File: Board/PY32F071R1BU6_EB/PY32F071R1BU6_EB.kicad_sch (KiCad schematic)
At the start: 2 parts, among them J7 Conn_02x05_Odd_Even, U1 PY32F071R1BU

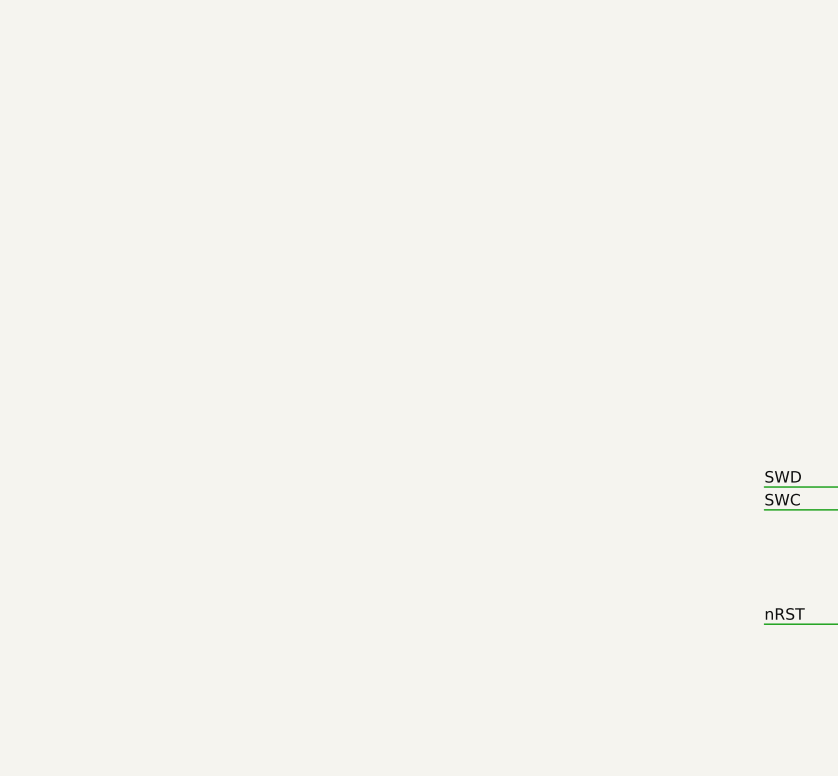
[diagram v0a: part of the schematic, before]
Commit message: Added USB connector
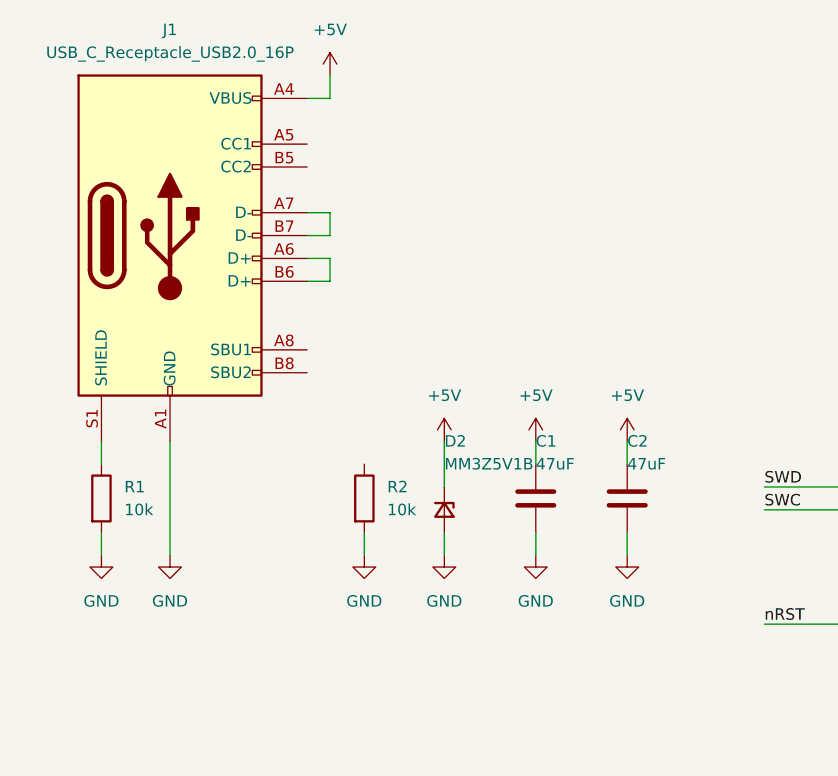
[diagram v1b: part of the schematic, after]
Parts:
- added C1, C2: 47uF, Capacitor_SMD:C_0805_2012Metric_Pad1.18x1.45mm_HandSolder, symbol Device:C
- added D2: MM3Z5V1B, Diode_SMD:D_SOD-323, symbol Device:D_Zener_Small
- added J1: USB_C_Receptacle_USB2.0_16P, Connector_USB:USB_C_Receptacle_HCTL_HC-TYPE-C-16P-01A, symbol Connector:USB_C_Receptacle_USB2.0_16P
- added R1, R2: 10k, Resistor_SMD:R_0603_1608Metric_Pad0.98x0.95mm_HandSolder, symbol Device:R
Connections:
- net +5V: now also C1.1, C2.1, D2.1 (K), J1.A4 (VBUS), J1.A9 (VBUS), J1.B4 (VBUS), J1.B9 (VBUS)
- net GND: now also C1.2, C2.2, D2.2 (A), J1.A1 (GND), J1.A12 (GND), J1.B1 (GND), J1.B12 (GND), R1.2, R2.2
- new net: J1.A6 (D+), J1.B6 (D+)
- new net: J1.A7 (D-), J1.B7 (D-)
- new net: J1.S1 (SHIELD), R1.1

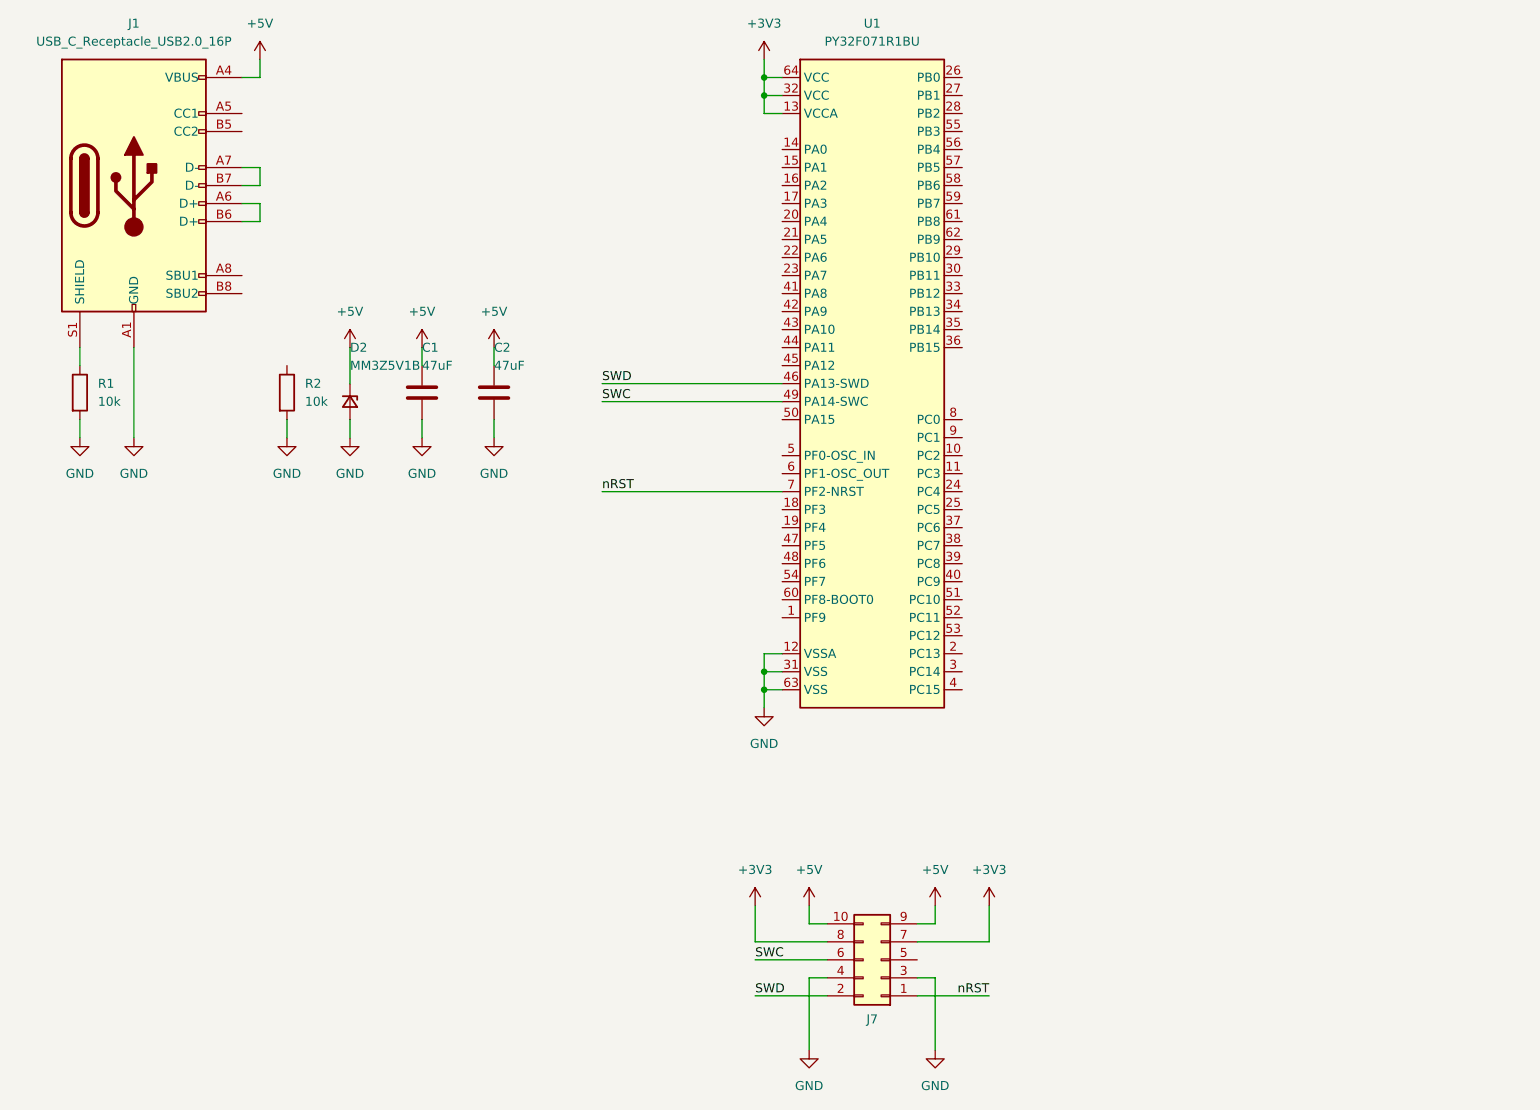
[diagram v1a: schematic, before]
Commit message: Kicad project was split in hierarchical sheets
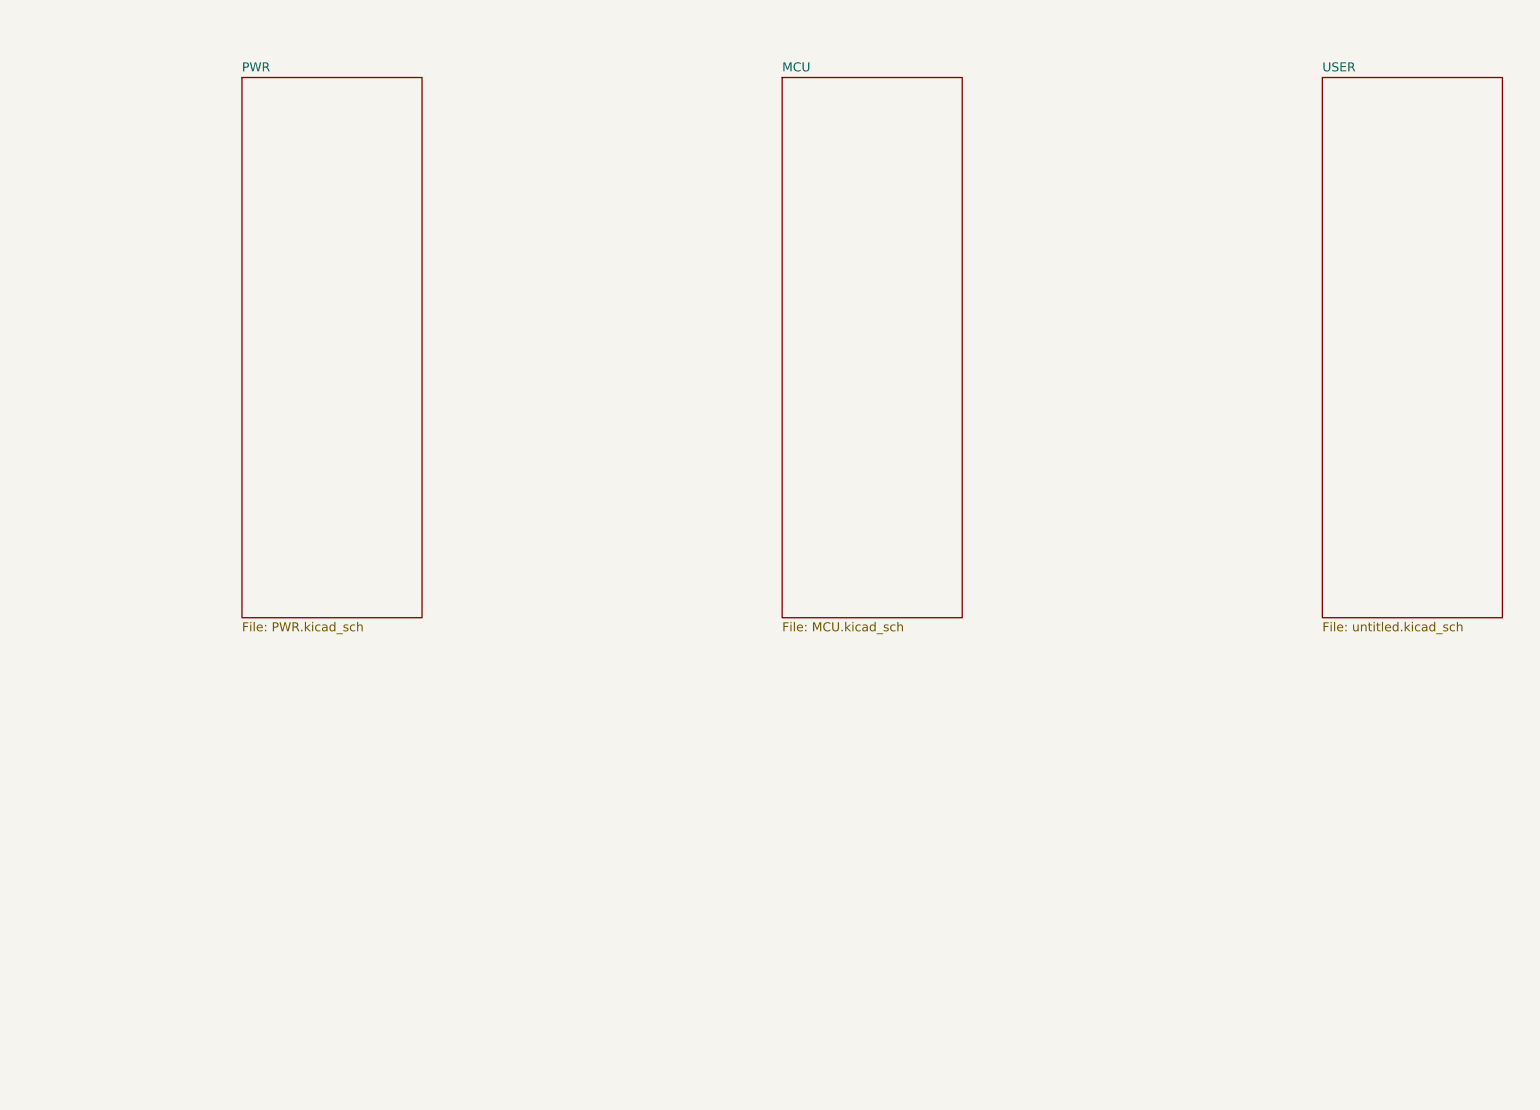
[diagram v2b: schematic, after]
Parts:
- removed C1, C2: 47uF, Capacitor_SMD:C_0805_2012Metric_Pad1.18x1.45mm_HandSolder, symbol Device:C
- removed D2: MM3Z5V1B, Diode_SMD:D_SOD-323, symbol Device:D_Zener_Small
- removed J1: USB_C_Receptacle_USB2.0_16P, Connector_USB:USB_C_Receptacle_HCTL_HC-TYPE-C-16P-01A, symbol Connector:USB_C_Receptacle_USB2.0_16P
- removed J7: Conn_02x05_Odd_Even, Connector_IDC:IDC-Header_2x05_P2.54mm_Vertical, symbol Connector_Generic:Conn_02x05_Odd_Even
- removed R1, R2: 10k, Resistor_SMD:R_0603_1608Metric_Pad0.98x0.95mm_HandSolder, symbol Device:R
- removed U1: PY32F071R1BU, Package_DFN_QFN:QFN-64-1EP_8x8mm_P0.4mm_EP6.5x6.5mm, symbol USER:PY32F071R1BU6
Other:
- added sheet MCU (MCU.kicad_sch)
- added sheet PWR (PWR.kicad_sch)
- added sheet USER (untitled.kicad_sch)

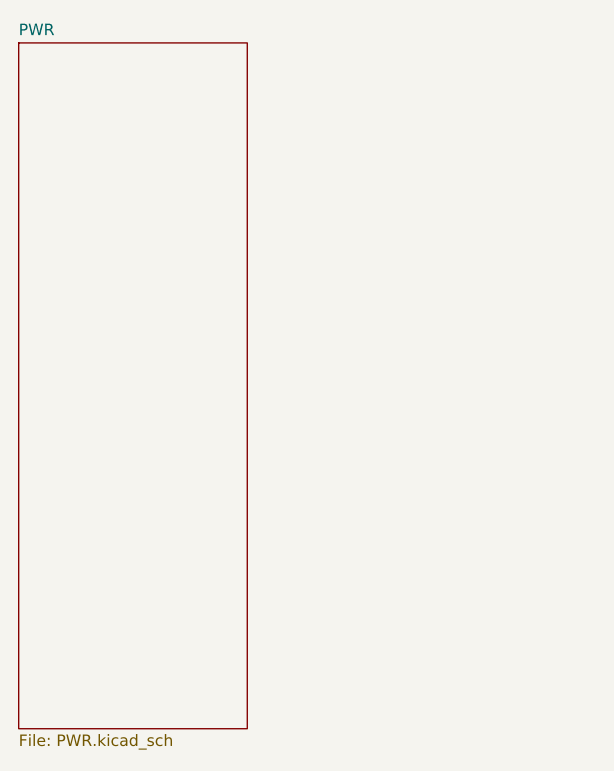
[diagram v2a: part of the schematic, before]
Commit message: Power circuit prepared
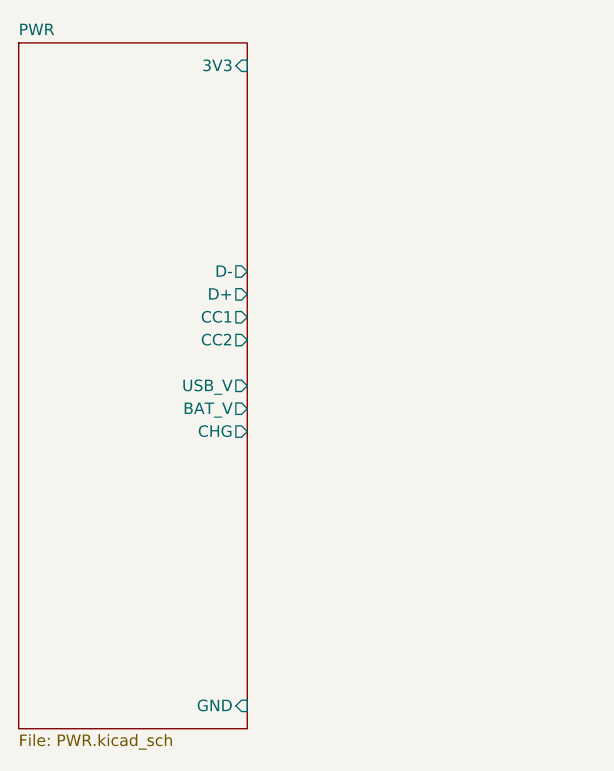
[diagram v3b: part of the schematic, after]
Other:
- sheet PWR ports: added 3V3, BAT_V, CC1, CC2, CHG, D+, D-, GND, USB_V; removed none
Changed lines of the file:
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@@
+			)
+		)
+		(pin "3V3" input
+			(at 76.2 53.34 0)
+			(effects
+				(font
+					(size 1.27 1.27)
+				)
+				(justify right)
+			)
+		)
+		(pin "GND" input
+			(at 76.2 124.46 0)
+			(effects
+				(font
+					(size 1.27 1.27)
+				)
+				(justify right)
+			)
+		)
+		(pin "D-" output
+			(at 76.2 76.2 0)
+			(effects
+				(font
+					(size 1.27 1.27)
+				)
+				(justify right)
+			)
+		)
+		(pin "D+" output
+			(at 76.2 78.74 0)
+			(effects
+				(font
+					(size 1.27 1.27)
+				)
+				(justify right)
+			)
+		)
+		(pin "CC2" output
+			(at 76.2 83.82 0)
+			(effects
+				(font
+					(size 1.27 1.27)
+				)
+				(justify right)
+			)
+		)
+		(pin "CC1" output
+			(at 76.2 81.28 0)
+			(effects
+				(font
+					(size 1.27 1.27)
+				)
+				(justify right)
+			)
+		)
+		(pin "CHG" output
+			(at 76.2 93.98 0)
+			(effects
+				(font
+					(size 1.27 1.27)
+				)
+				(justify right)
+			)
+		)
+		(pin "USB_V" output
+			(at 76.2 88.9 0)
+			(effects
+				(font
+					(size 1.27 1.27)
+				)
+				(justify right)
+			)
+		)
+		(pin "BAT_V" output
+			(at 76.2 91.44 0)
+			(effects
+				(font
+					(size 1.27 1.27)
+				)
+				(justify right)
 			)
 		)

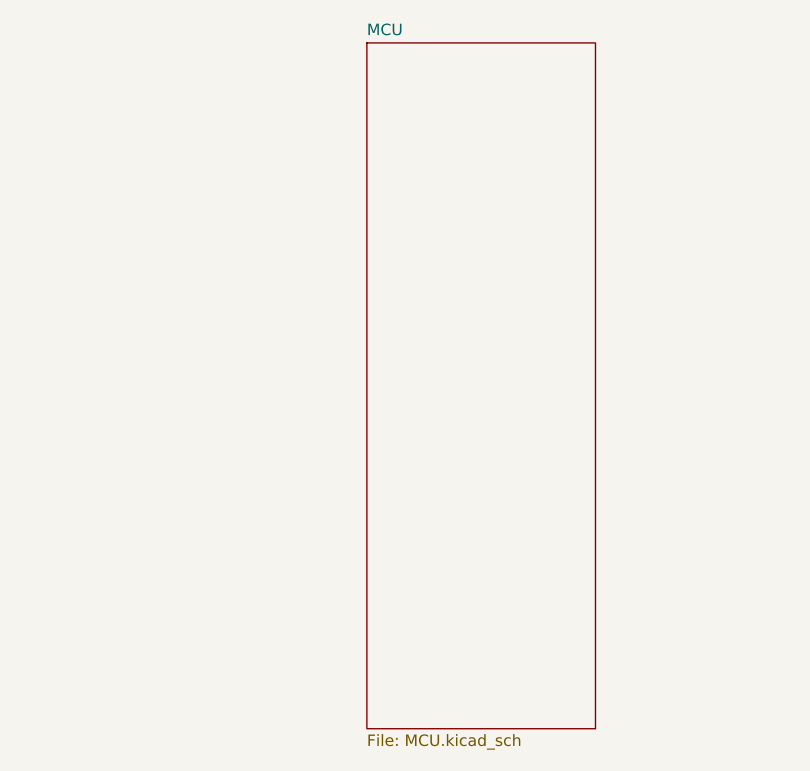
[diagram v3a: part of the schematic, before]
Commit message: Display added to schematic
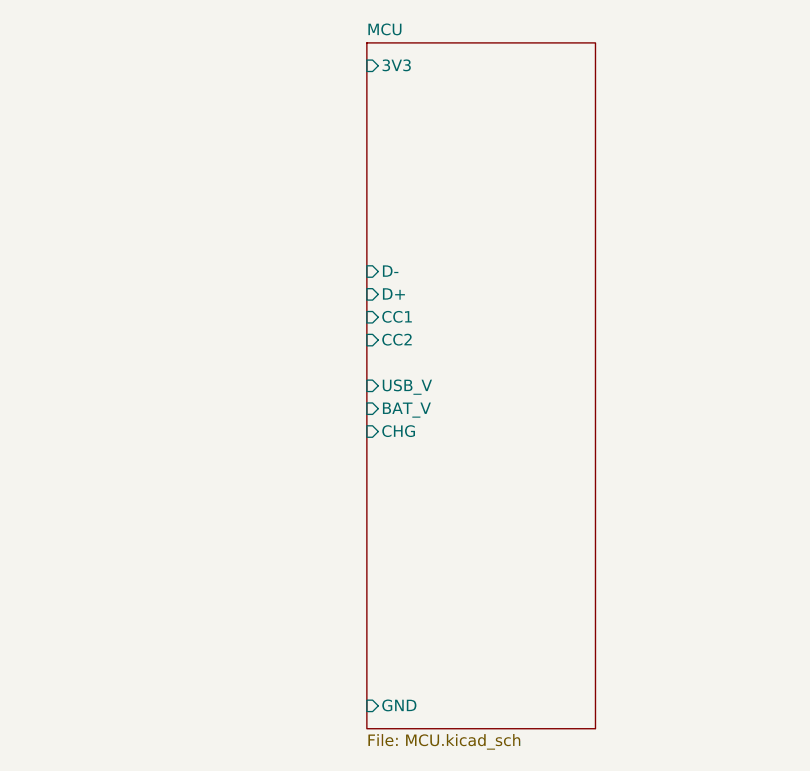
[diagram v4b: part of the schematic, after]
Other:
- sheet MCU ports: added 3V3, BAT_V, CC1, CC2, CHG, D+, D-, GND, USB_V; removed none
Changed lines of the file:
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@@
+			)
+		)
+		(pin "3V3" input
+			(at 127 53.34 180)
+			(effects
+				(font
+					(size 1.27 1.27)
+				)
+				(justify left)
+			)
+		)
+		(pin "D-" input
+			(at 127 76.2 180)
+			(effects
+				(font
+					(size 1.27 1.27)
+				)
+				(justify left)
+			)
+		)
+		(pin "D+" input
+			(at 127 78.74 180)
+			(effects
+				(font
+					(size 1.27 1.27)
+				)
+				(justify left)
+			)
+		)
+		(pin "USB_V" input
+			(at 127 88.9 180)
+			(effects
+				(font
+					(size 1.27 1.27)
+				)
+				(justify left)
+			)
+		)
+		(pin "CC1" input
+			(at 127 81.28 180)
+			(effects
+				(font
+					(size 1.27 1.27)
+				)
+				(justify left)
+			)
+		)
+		(pin "CHG" input
+			(at 127 93.98 180)
+			(effects
+				(font
+					(size 1.27 1.27)
+				)
+				(justify left)
+			)
+		)
+		(pin "CC2" input
+			(at 127 83.82 180)
+			(effects
+				(font
+					(size 1.27 1.27)
+				)
+				(justify left)
+			)
+		)
+		(pin "BAT_V" input
+			(at 127 91.44 180)
+			(effects
+				(font
+					(size 1.27 1.27)
+				)
+				(justify left)
+			)
+		)
+		(pin "GND" input
+			(at 127 124.46 180)
+			(effects
+				(font
+					(size 1.27 1.27)
+				)
+				(justify left)
 			)
 		)

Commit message: Schematic updated
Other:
- sheet MCU ports: added BLK, BTN0, BTN1, BTN2, CSX, D0, DCX, FREQ, LED0, LED1, LED2, RESX, SCL; removed none
- sheet USER ports: added 3V3, BLK, BTN0, BTN1, BTN2, CSX, D0, DCX, FREQ, GND, LED0, LED1, LED2, RESX, SCL; removed none

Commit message: Component placement started
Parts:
- added H1, H2, H3, H4: MountingHole_Pad, MountingHole:MountingHole_4.3mm_M4_Pad, symbol Mechanical:MountingHole_Pad
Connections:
- new net GND: H1.1, H2.1, H3.1, H4.1
